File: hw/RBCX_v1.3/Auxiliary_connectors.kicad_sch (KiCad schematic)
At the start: 20 parts, among them J24 Conn_01x06, J25 Conn_01x06, J26 Conn_01x06, J27 Conn_01x04, J28 Conn_01x06

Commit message: Production files
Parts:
- J24, J25, J26, J28: JLCPCB_CORRECTION (none) -> 0;-6.35;90
- J27: JLCPCB_CORRECTION (none) -> 0;-3.81;90
- TP10: JLCPCB_IGNORE (none) -> 1
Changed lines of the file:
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@@
+      (effects (font (size 1.27 1.27)) hide)
+    )
+    (property "JLCPCB_CORRECTION" "0;-6.35;90" (id 6) (at 106.68 68.58 0)
       (effects (font (size 1.27 1.27)) hide)
     )
@@
       (effects (font (size 1.27 1.27)) hide)
     )
+    (property "JLCPCB_CORRECTION" "0;-6.35;90" (id 6) (at 106.68 93.98 0)
+      (effects (font (size 1.27 1.27)) hide)
+    )
     (pin "1")
     (pin "2")
@@
       (effects (font (size 1.27 1.27)) hide)
     )
+    (property "JLCPCB_CORRECTION" "0;-3.81;90" (id 6) (at 204.47 83.693 0)
+      (effects (font (size 1.27 1.27)) hide)
+    )
     (pin "1")
     (pin "2")
@@
     )
     (property "Datasheet" "" (id 3) (at 69.85 60.96 0)
+      (effects (font (size 1.27 1.27)) hide)
+    )
+    (property "JLCPCB_IGNORE" "1" (id 4) (at 69.85 60.96 0)
       (effects (font (size 1.27 1.27)) hide)
     )
@@
       (effects (font (size 1.27 1.27)) hide)
     )
+    (property "JLCPCB_CORRECTION" "0;-6.35;90" (id 6) (at 204.47 60.96 0)
+      (effects (font (size 1.27 1.27)) hide)
+    )
     (pin "1")
     (pin "2")
@@
       (effects (font (size 1.27 1.27)) hide)
     )
+    (property "JLCPCB_CORRECTION" "0;-6.35;90" (id 6) (at 251.46 60.96 0)
+      (effects (font (size 1.27 1.27)) hide)
+    )

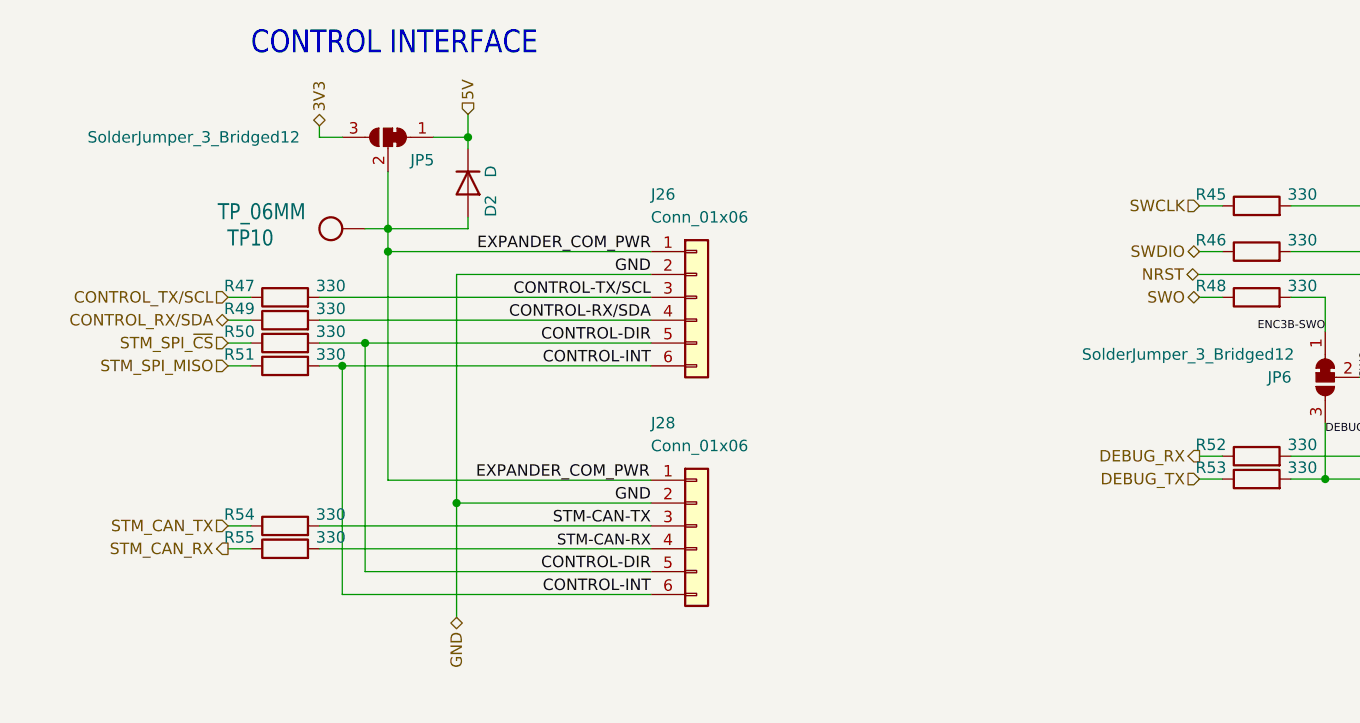
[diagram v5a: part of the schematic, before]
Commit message: Kuba issues
Change of power transistor from JSM3622 to JMSL0302AU

NTC connectors

Moving the Cell balancer behind the switch

and some little things
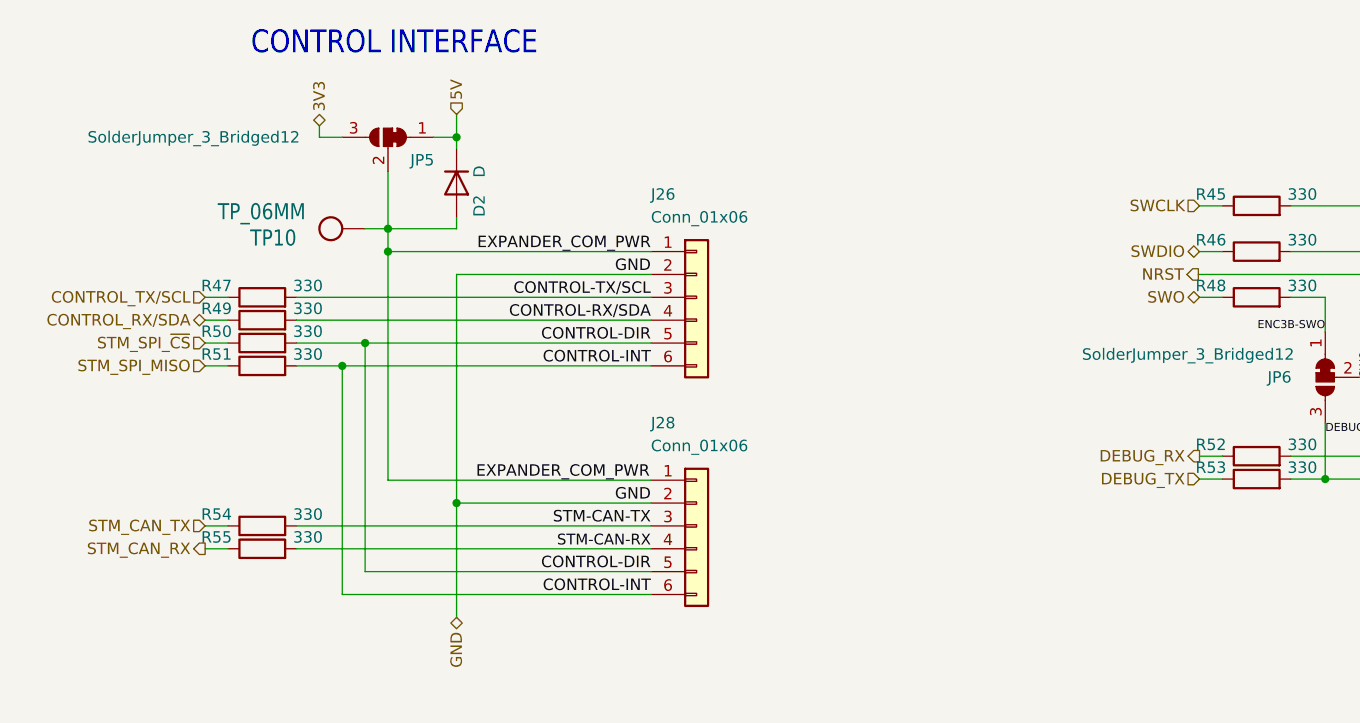
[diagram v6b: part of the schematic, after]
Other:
- moved on the sheet: D2, R47, R49, R50, R51, R54, R55
